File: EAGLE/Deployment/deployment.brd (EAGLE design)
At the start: 160 x 100 mm, 10 parts, among them Q1 100V 14A, Q2 100V 14A

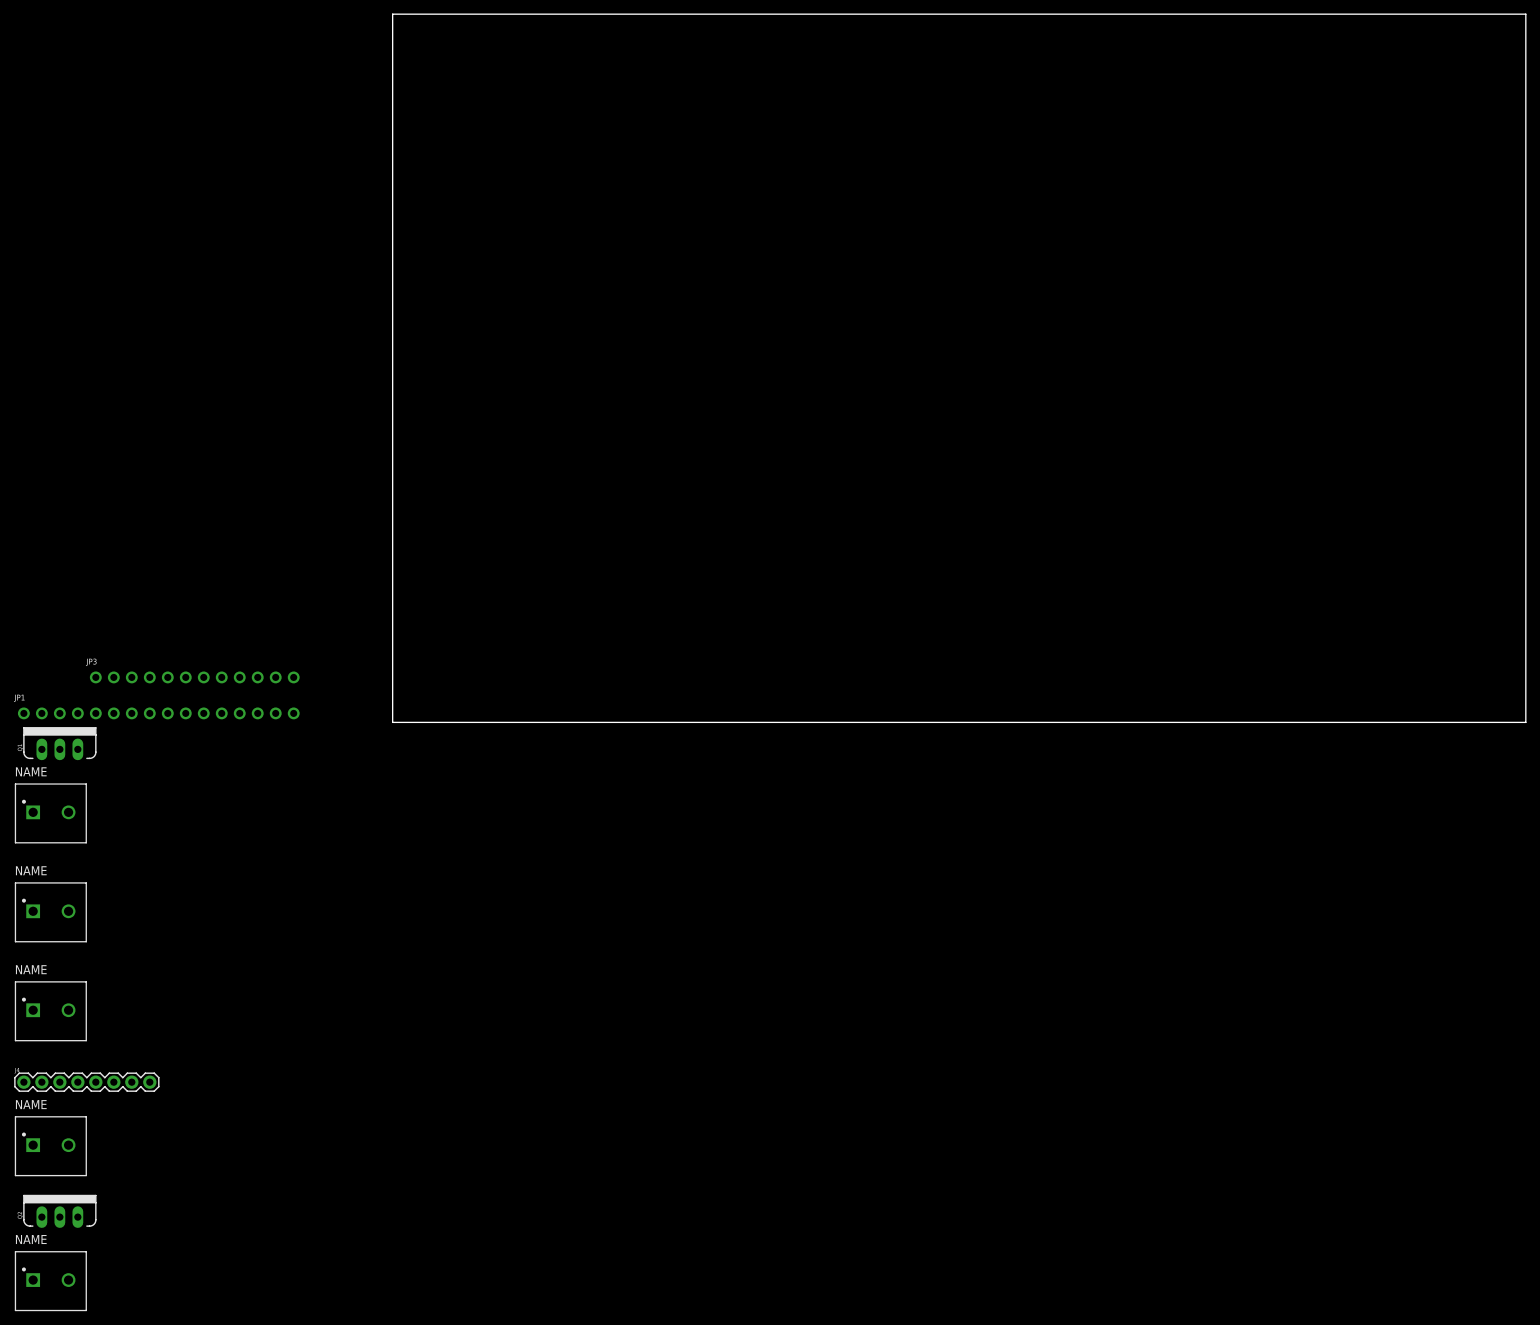
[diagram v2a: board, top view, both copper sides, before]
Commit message: starts full scale deployment circuitboard, neeeds design review and imu
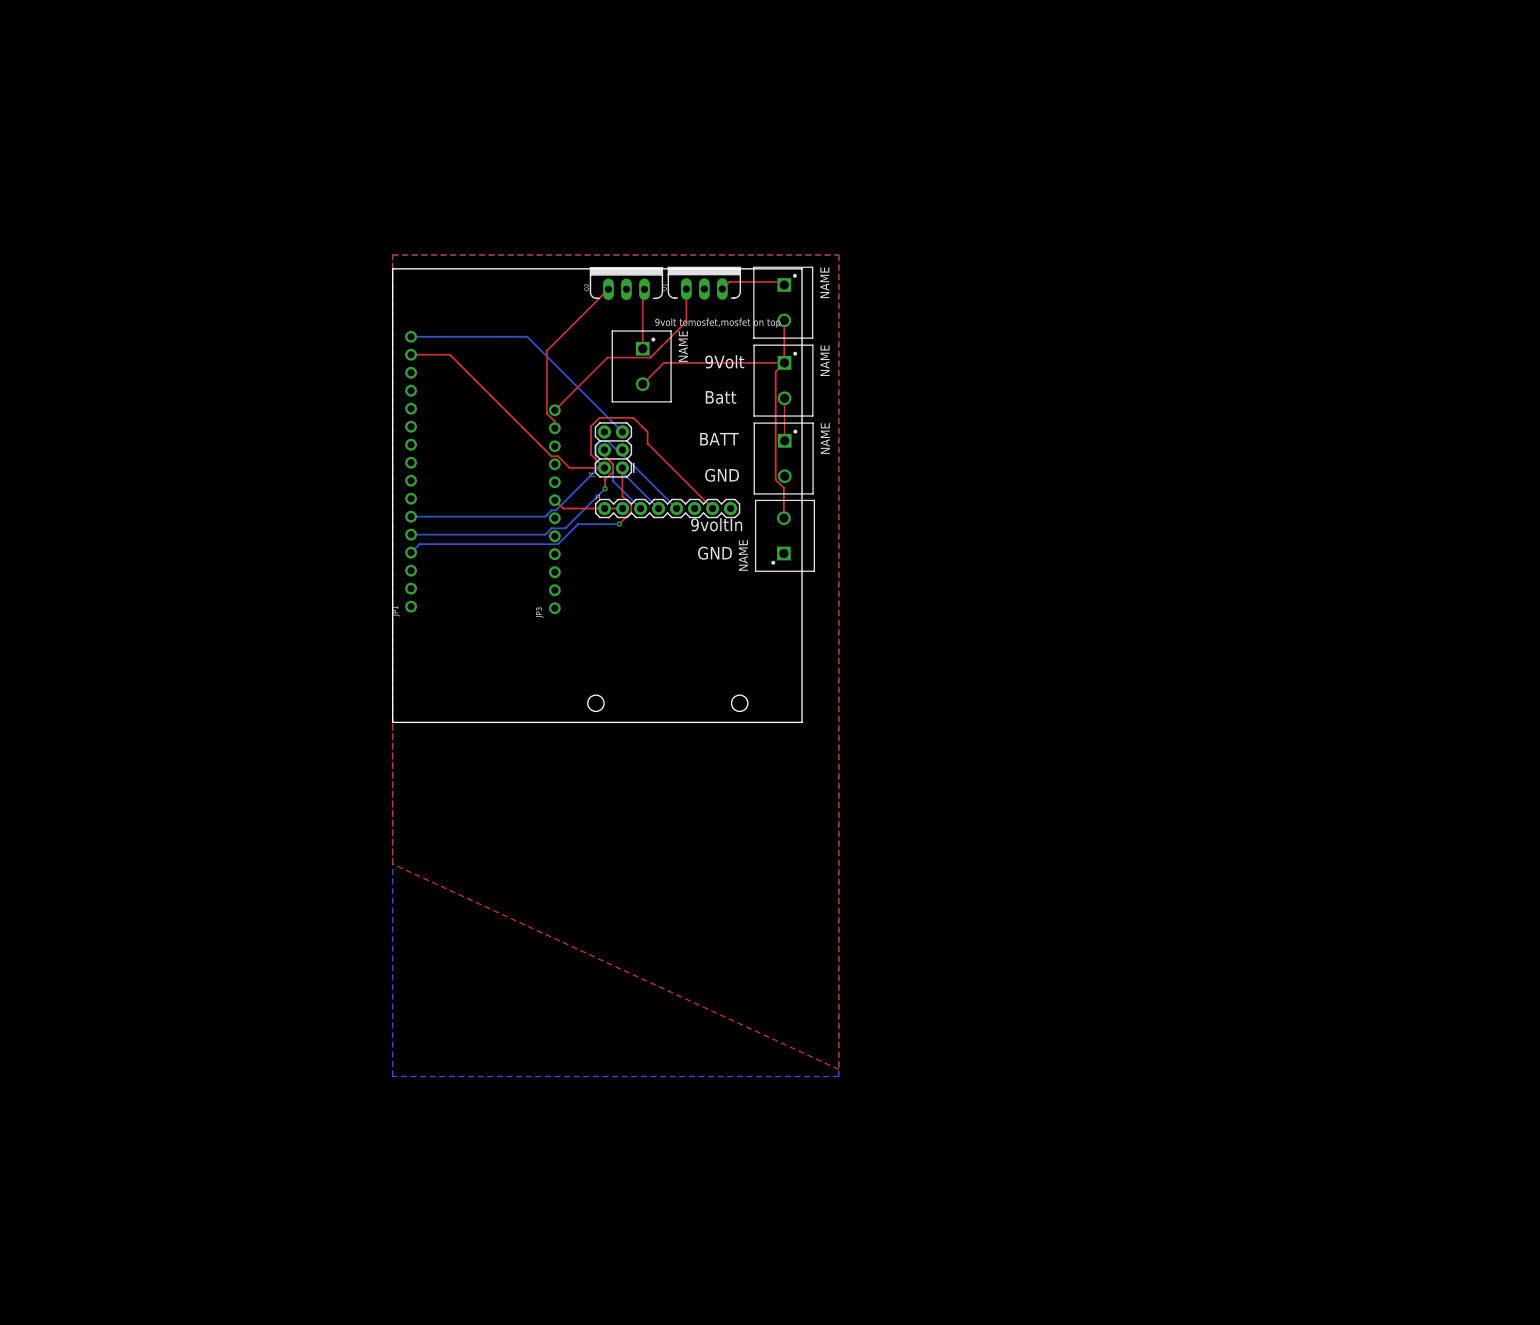
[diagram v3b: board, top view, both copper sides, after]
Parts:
- added J7: AVR_SPI_PROG_3X2PTH, SparkFun-Connectors:2X3
- moved Q2 153.5 mm to (33.0, 61.1)
- moved J6 147.5 mm to (55.2, 26.3), turned to 90 degrees
- moved J5 138.1 mm to (35.3, 50.3), turned to 270 degrees
- moved J3 129.6 mm to (55.4, 37.3), turned to 270 degrees
- moved J2 127.8 mm to (55.3, 48.3), turned to 270 degrees
- moved J1 126.1 mm to (55.3, 59.3), turned to 270 degrees
- moved J4 115.3 mm to (29.9, 30.2)
- moved Q1 111.8 mm to (44.0, 61.2)
- moved JP3 56.1 mm to (22.9, 30.1), turned to 90 degrees
- moved JP1 49.3 mm to (2.60, 35.4), turned to 90 degrees
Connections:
- net +3V3: now also J7.2
- net GND: now also J7.6
- net MISO: now also J7.1
- net MOSI: now also J7.4
- net RST: now also J7.5
- net SCK: now also J7.3
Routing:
- net +3V3: track 0.00 -> 64.5 mm
- net 9V: track 0.00 -> 50.2 mm
- net SCK: track 0.00 -> 48.2 mm
- net MISO: track 0.00 -> 48.1 mm, vias 0 -> 1
- net MOSI: track 0.00 -> 46.9 mm, vias 0 -> 1
- net RST: track 0.00 -> 35.4 mm
- net 2: track 0.00 -> 28.4 mm
- net 3: track 0.00 -> 23.7 mm
- net 10: track 0.00 -> 10.1 mm
- net N$1: track 0.00 -> 9.34 mm
- net N$2: track 0.00 -> 8.49 mm
- net BATT+: track 0.00 -> 6.01 mm
- added copper zone on layer 1, net GND
- added copper zone on layer 16, net GND
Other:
- board size 160 x 100 mm -> 57.8 x 64 mm
- board text added: "9Volt"
- board text added: "9volt tomosfet,mosfet on top"
- board text added: "9voltIn"
- board text added: "BATT"
- board text added: "Batt"
- board text added: "GND"
